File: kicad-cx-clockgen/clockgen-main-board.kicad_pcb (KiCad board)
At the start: 2 copper layers, 70 x 64.4 mm, 35 parts, among them J1 Headswitch_SMA, J10 Conn_01x01_Pin, J11 Conn_01x01_Pin, J12 Conn_01x01_Pin, J13 Conn_01x01_Pin, J14 Conn_Coaxial, J2 Conn_Coaxial, J3 Conn_01x03_Pin, J4 Conn_01x03_Pin, J5 Conn_01x01_Pin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

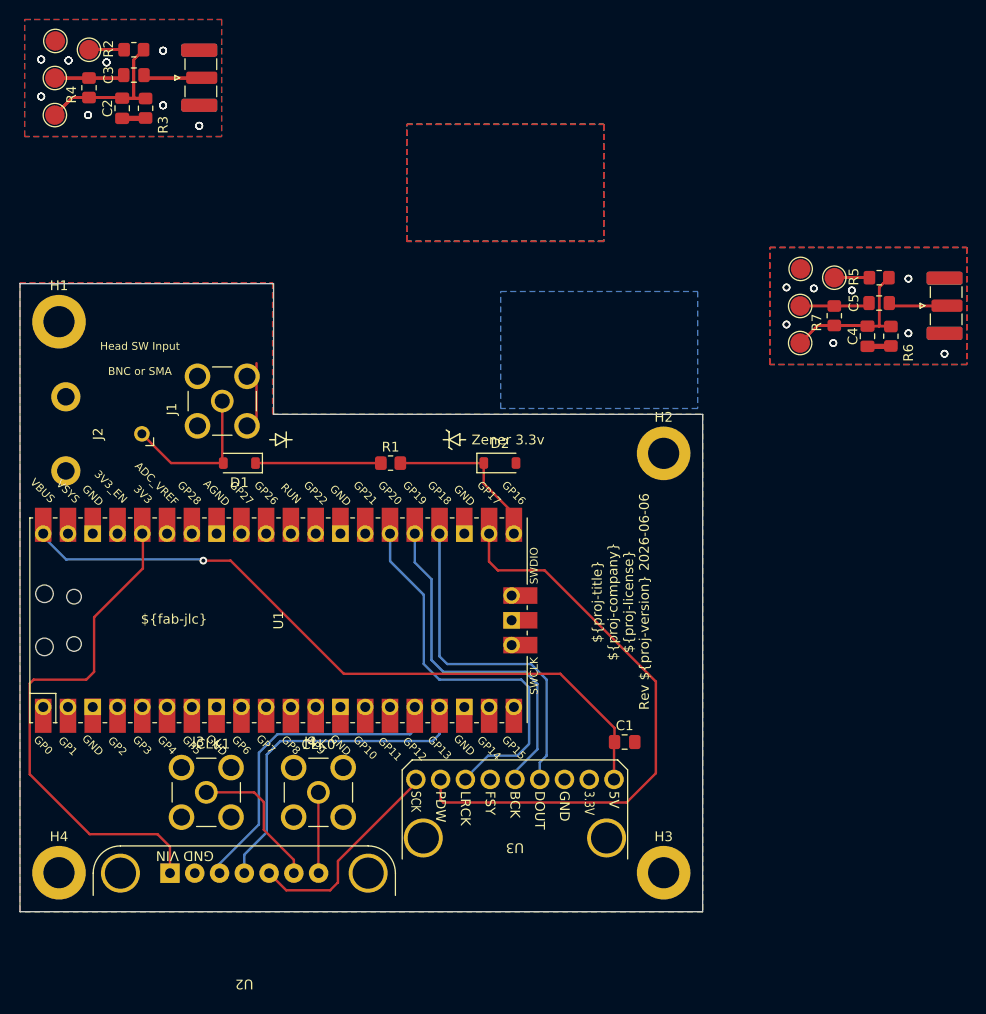
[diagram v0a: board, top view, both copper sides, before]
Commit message: refactor: Split combined main board + jig project into discrete ones
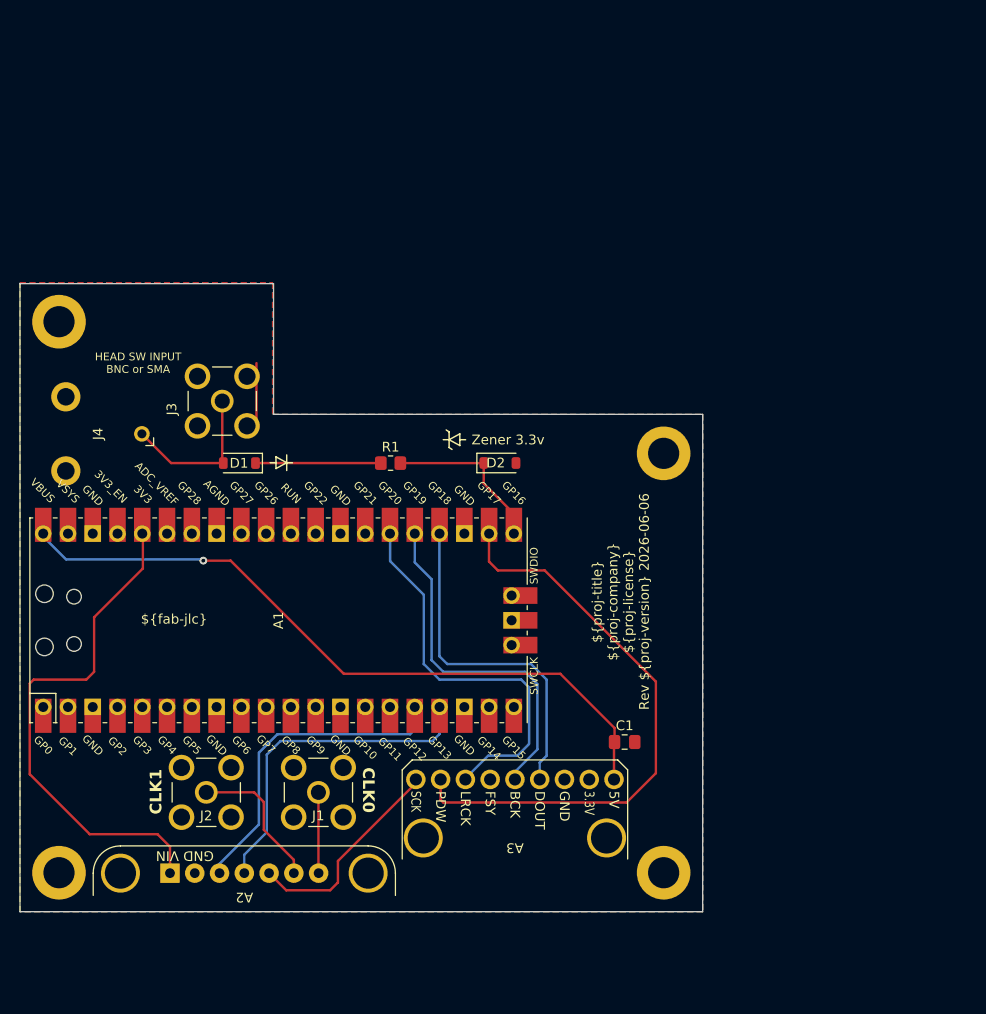
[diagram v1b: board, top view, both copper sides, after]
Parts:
- removed C2, C4: 10n, Capacitor_SMD:C_0805_2012Metric_Pad1.18x1.45mm_HandSolder
- removed C3, C5: 1n5, Capacitor_SMD:C_0805_2012Metric_Pad1.18x1.45mm_HandSolder
- removed J10, J11, J12, J13, J5, J6, J7, J8: Conn_01x01_Pin, TestPoint:TestPoint_Pad_D2.0mm
- removed J14, J9: Conn_Coaxial, Connector_Coaxial:SMA_Samtec_SMA-J-P-H-ST-EM1_EdgeMount
- removed R2, R3, R5, R6: 1k, Resistor_SMD:R_0805_2012Metric_Pad1.20x1.40mm_HandSolder
- removed R4, R7: 10k, Resistor_SMD:R_0805_2012Metric_Pad1.20x1.40mm_HandSolder
- A2: renamed from U2; value ~ -> Si5351A
- A3: renamed from U3; value ~ -> PCM1802
- J1: renamed from J4; value Conn_01x03_Pin -> CLK0_SMA
- J2: renamed from J3; value Conn_01x03_Pin -> CLK1_SMA
- J4: renamed from J2; value Conn_Coaxial -> Headswitch_BNC
- renumbered U1 to A1, J1 to J3
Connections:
- net /Main Board/Gen.SCL renamed /Gen.SCL
- net /Main Board/Gen.SDA renamed /Gen.SDA
- net /Main Board/Gen.VSI renamed /Gen.VSI
- net /Main Board/Head_SW_In renamed /Head_SW_In
- net /Main Board/PCM.5V renamed /PCM.5V
- net /Main Board/PCM.BitClk renamed /PCM.BitClk
- net /Main Board/PCM.Data renamed /PCM.Data
- net /Main Board/PCM.LRClk renamed /PCM.LRClk
- net /Main Board/PCM.PwrDn renamed /PCM.PwrDn
- net /Main Board/PCM.SysClk renamed /PCM.SysClk
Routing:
- net /HiFi Audio CX Jig/XT2: track 62.1 -> 0.00 mm
- net /Video CX Jig/XT2: track 31.0 -> 0.00 mm
- net /HiFi Audio CX Jig/XT1: track 28.7 -> 0.00 mm
- net Net-(J9-In): track 20.2 -> 0.00 mm
- net GND: track 21.6 -> 6.80 mm, vias 48 -> 0
- net /HiFi Audio CX Jig/V_{cc}_3V3: track 14.4 -> 0.00 mm
- net /Video CX Jig/XT1: track 14.4 -> 0.00 mm
- net Net-(J14-In): track 10.1 -> 0.00 mm
- net /Video CX Jig/V_{cc}_3V3: track 7.20 -> 0.00 mm
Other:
- board text added: "HEAD SW INPUT BNC or SMA"
- board text removed: "Head SW Input BNC or SMA"
